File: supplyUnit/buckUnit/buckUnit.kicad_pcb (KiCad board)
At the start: 2 copper layers, 72.7 x 33.9 mm, 30 parts, among them J1 VBAT, J2 Motor, J3 Dribbler A, J4 Conn_01x05, J5 L1, J6 Conn_02x03_Counter_Clockwise, J7 Conn_02x03_Counter_Clockwise, J8 Dribbler B, Q1 BSC084P03NS3 G, Q2 BSC084P03NS3 G, Q3 IRLML6344TRPbF, SW1 SW_SPDT, U1 OKL-T6-W12-C, U2 OKL-T6-W12-C

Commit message: 死
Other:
- board text added: "JLCJLCJLCJLC"

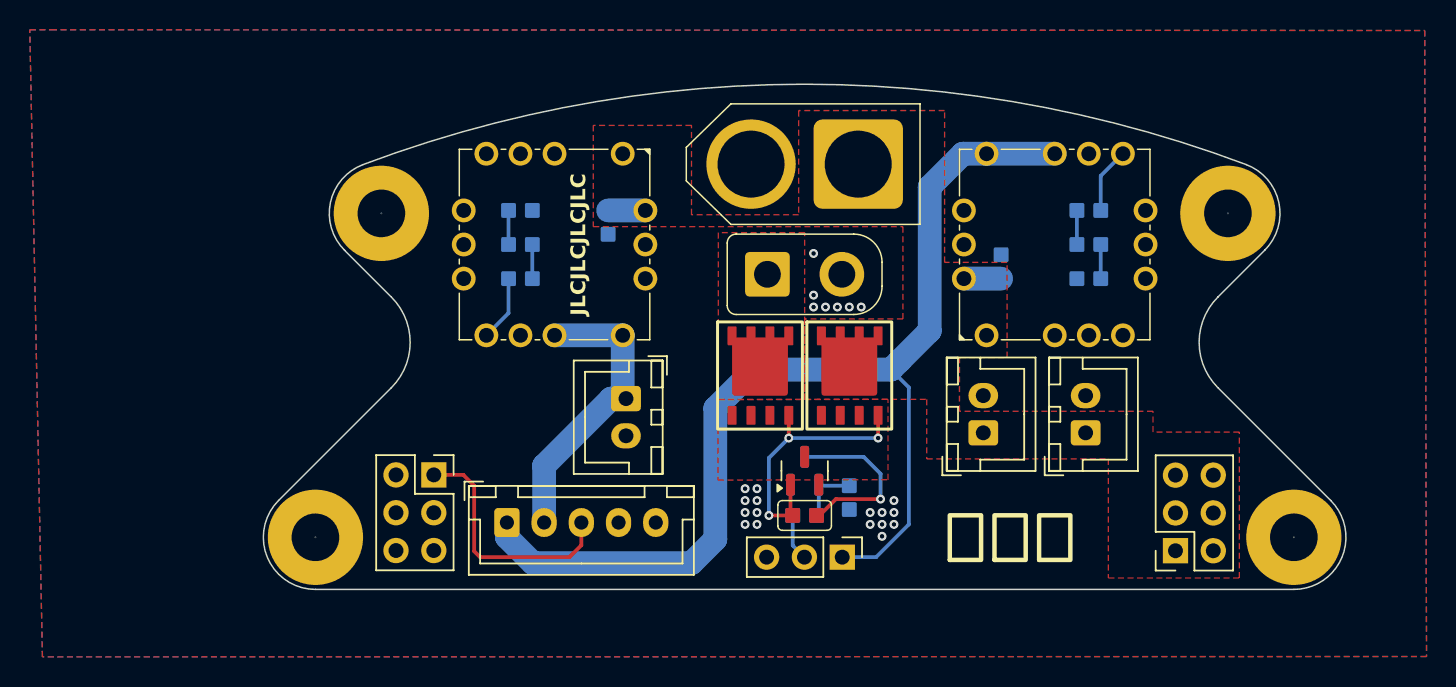
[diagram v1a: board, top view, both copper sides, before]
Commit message: 死 - 过杀 PMOS
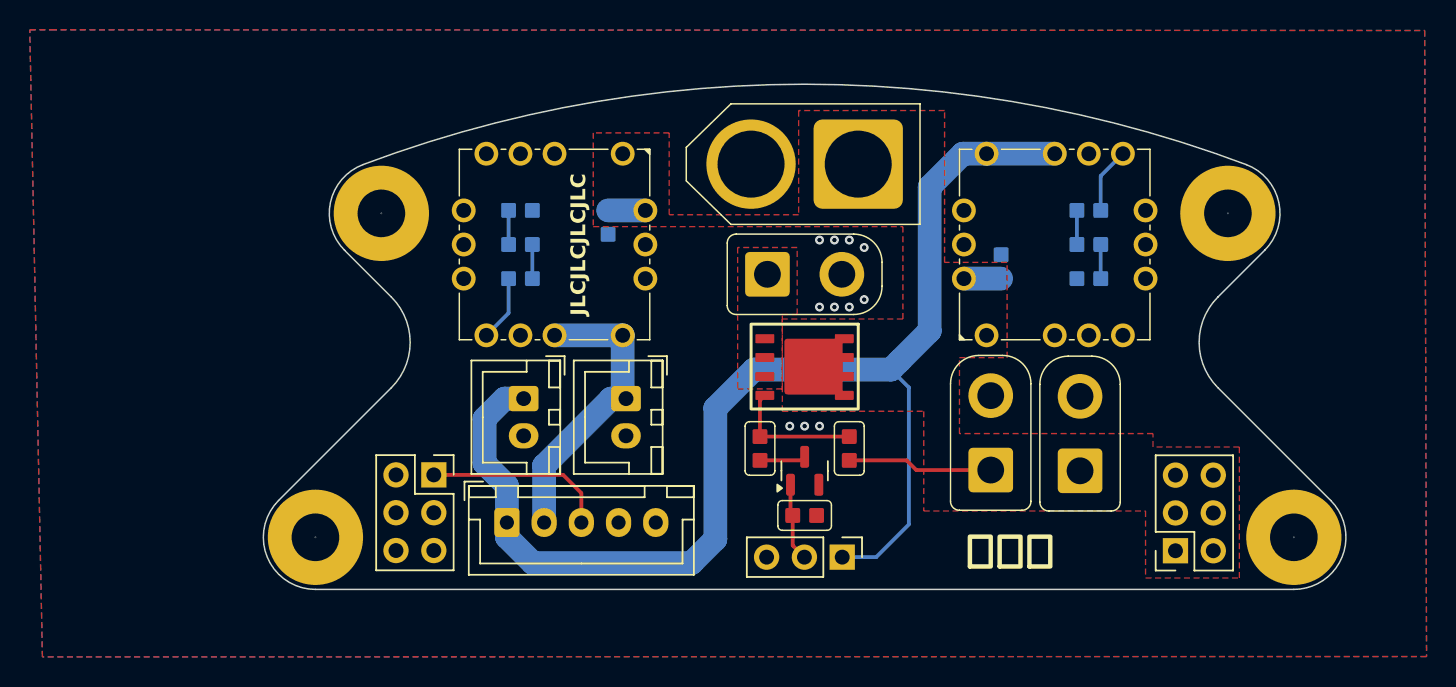
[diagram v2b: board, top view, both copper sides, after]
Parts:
- removed D1: BZX84C12, Package_TO_SOT_SMD:SOT-23
- removed Q3: IRLML6344TRPbF, Package_TO_SOT_SMD:SOT-23
- added J9: SPARE, Connector_JST:JST_XH_B2B-XH-A_1x02_P2.50mm_Vertical, F.Cu at (118.3, 105.5)
- J3, J8: footprint Connector_JST:JST_XH_B2B-XH-A_1x02_P2.50mm_Vertical -> Library:xt30-f
- Q2: value BSC084P03NS3 G -> IRLML6344TRPbF; footprint Library:8-DFN (5x6) -> Package_TO_SOT_SMD:SOT-23
- R8: value 10K -> 100; moved to F.Cu
- R9: moved to F.Cu
- moved Q2 7.07 mm to (137.2, 110.4), turned to 90 degrees
- moved R7 5.41 mm to (140.2, 108.9), turned to 90 degrees
- moved R8 5.41 mm to (134.2, 108.9), turned to -90 degrees
- moved R9 3.23 mm to (137.2, 113.4), turned to 0 degrees
- moved Q1 3.06 mm to (137.2, 103.4), turned to -90 degrees
- moved J3 0.50 mm to (149.7, 107.8)
- moved J8 0.38 mm to (155.7, 107.9)
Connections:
- Q1 pad 1: Net-(D1-K) -> +12V MOTOR
- Q1 pad 2: Net-(D1-K) -> +12V MOTOR
- Q1 pad 3: Net-(D1-K) -> +12V MOTOR
- Q1 pad 4: Net-(D1-A) -> Net-(Q1-G)
- Q2 pad 1: Net-(D1-K) -> Net-(Q2-G)
- Q2 pad 2: Net-(D1-K) -> GND
- Q2 pad 3: Net-(D1-K) -> Net-(Q2-D)
- R7 pad 1: Net-(D1-A) -> +12V
- R7 pad 2: Net-(Q3-D) -> Net-(Q1-G)
- R8 pad 1: Net-(SW1-B) -> Net-(Q1-G)
- R8 pad 2: Net-(Q3-G) -> Net-(Q2-D)
- R9 pad 1: Net-(Q3-G) -> Net-(Q2-G)
- SW1 pad 2: Net-(SW1-B) -> Net-(Q2-G)
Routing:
- net Net-(D1-A): track 18.3 -> 0.00 mm, vias 3 -> 0
- net Net-(Q3-D): track 12.1 -> 0.00 mm, vias 1 -> 0
- net +5V: track 77.0 -> 87.8 mm
- net +12V: track 5.00 -> 14.8 mm
- net Net-(Q1-G): track 0.00 -> 8.90 mm
- net Net-(Q2-G): track 0.00 -> 5.25 mm
- net /KICK SIG: track 16.6 -> 12.4 mm
- net Net-(Q3-G): track 3.90 -> 0.00 mm
- net Net-(SW1-B): track 3.13 -> 0.00 mm
- net Net-(Q2-D): track 0.00 -> 3.10 mm
- net GND: vias 23 -> 11
- removed copper zone on F.Cu, net Net-(D1-K)

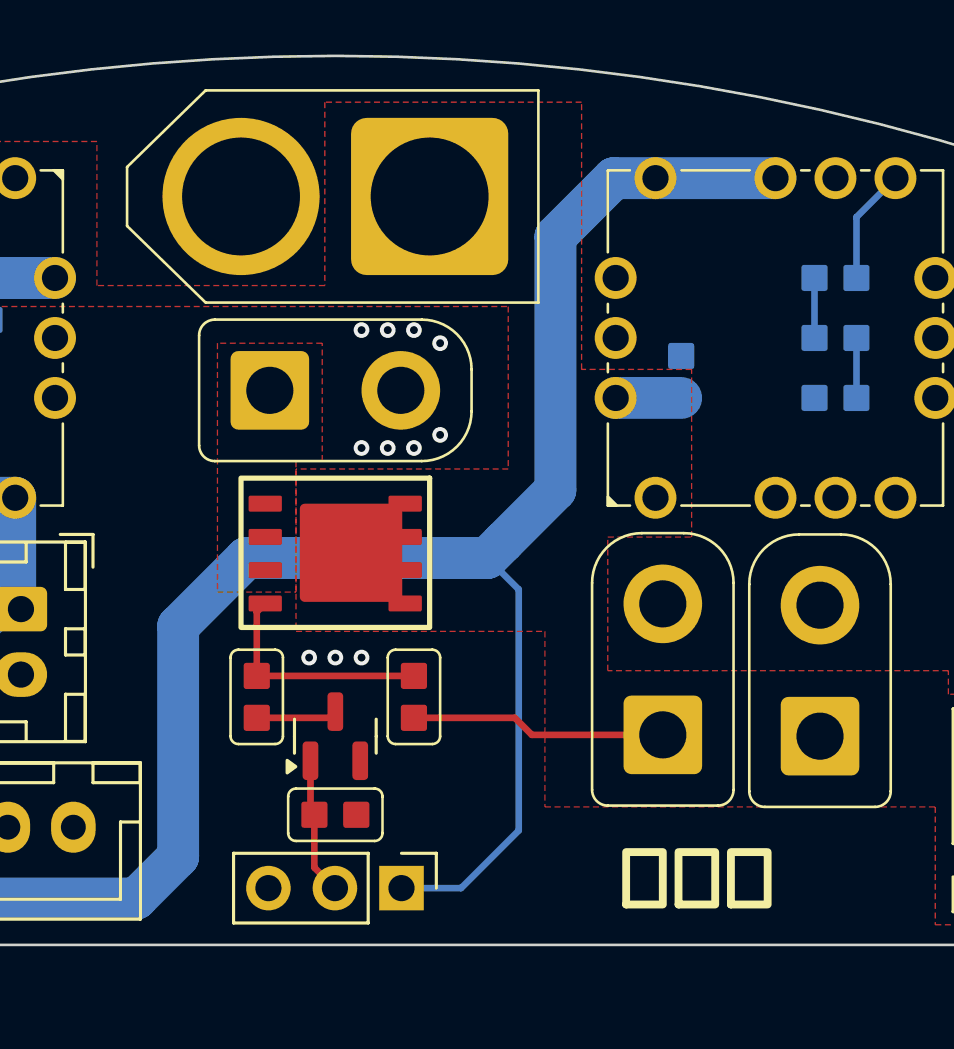
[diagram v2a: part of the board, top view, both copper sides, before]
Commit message: 死 - 过杀 PMOS
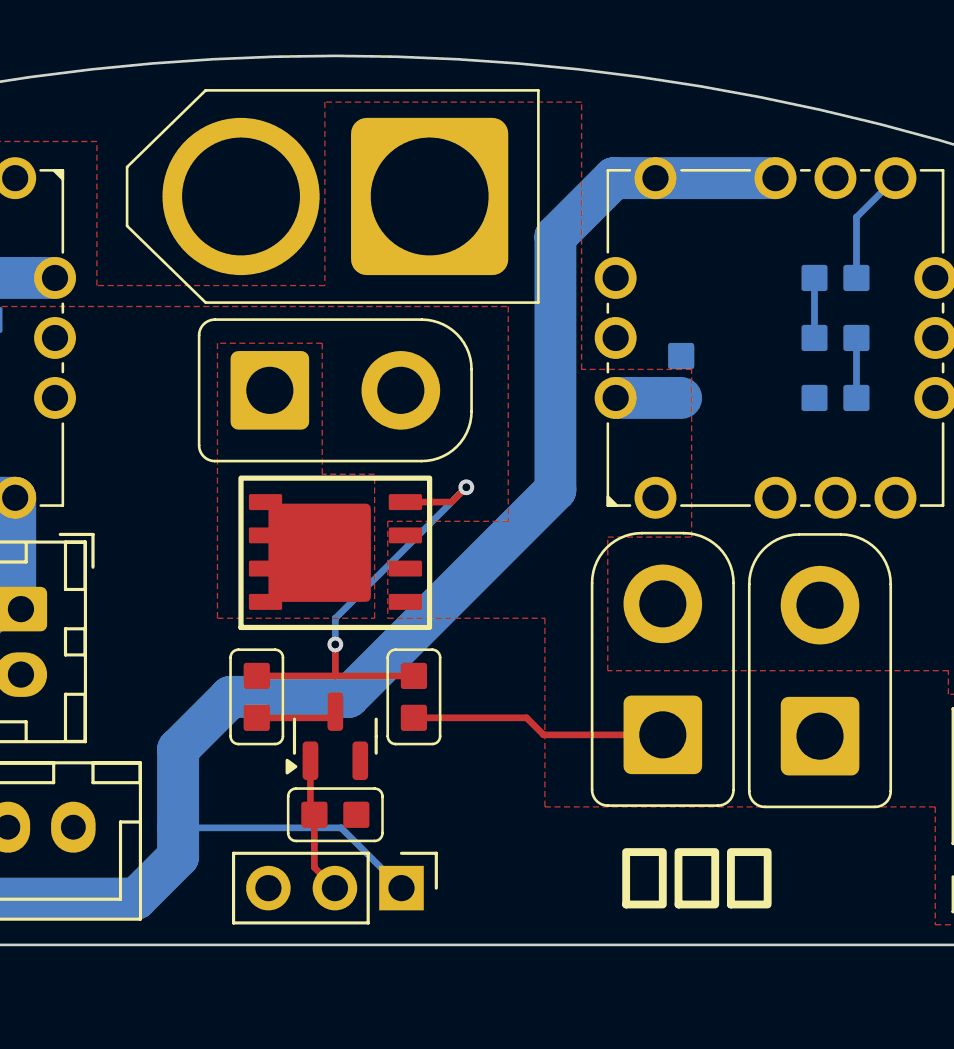
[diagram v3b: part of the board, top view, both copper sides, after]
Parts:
- R8: value 100 -> 1K
- U1, U2: value OKL-T6-W12-C -> OKL-T6-W12P-C
- turned Q1 to 90 degrees
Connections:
- Q1 pad 1: +12V MOTOR -> +12V
- Q1 pad 2: +12V MOTOR -> +12V
- Q1 pad 3: +12V MOTOR -> +12V
- Q1 pad 5: +12V -> +12V MOTOR
- Q1 pad 6: +12V -> +12V MOTOR
- Q1 pad 7: +12V -> +12V MOTOR
- Q1 pad 8: +12V -> +12V MOTOR
- Q1 pad 9: +12V -> +12V MOTOR
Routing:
- net +5V: track 87.8 -> 78.2 mm
- net Net-(Q1-G): track 8.90 -> 17.8 mm, vias 0 -> 2
- net GND: vias 11 -> 0

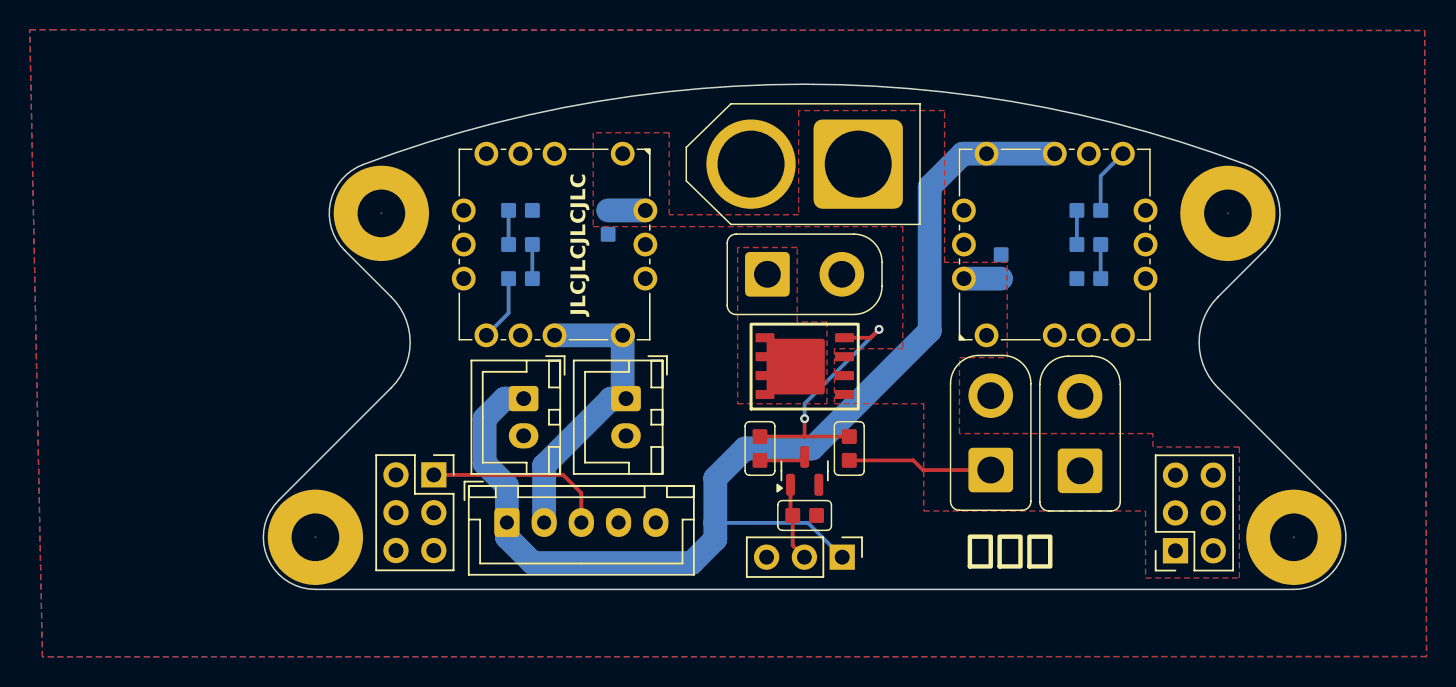
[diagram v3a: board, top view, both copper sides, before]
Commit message: Going to move to VNH
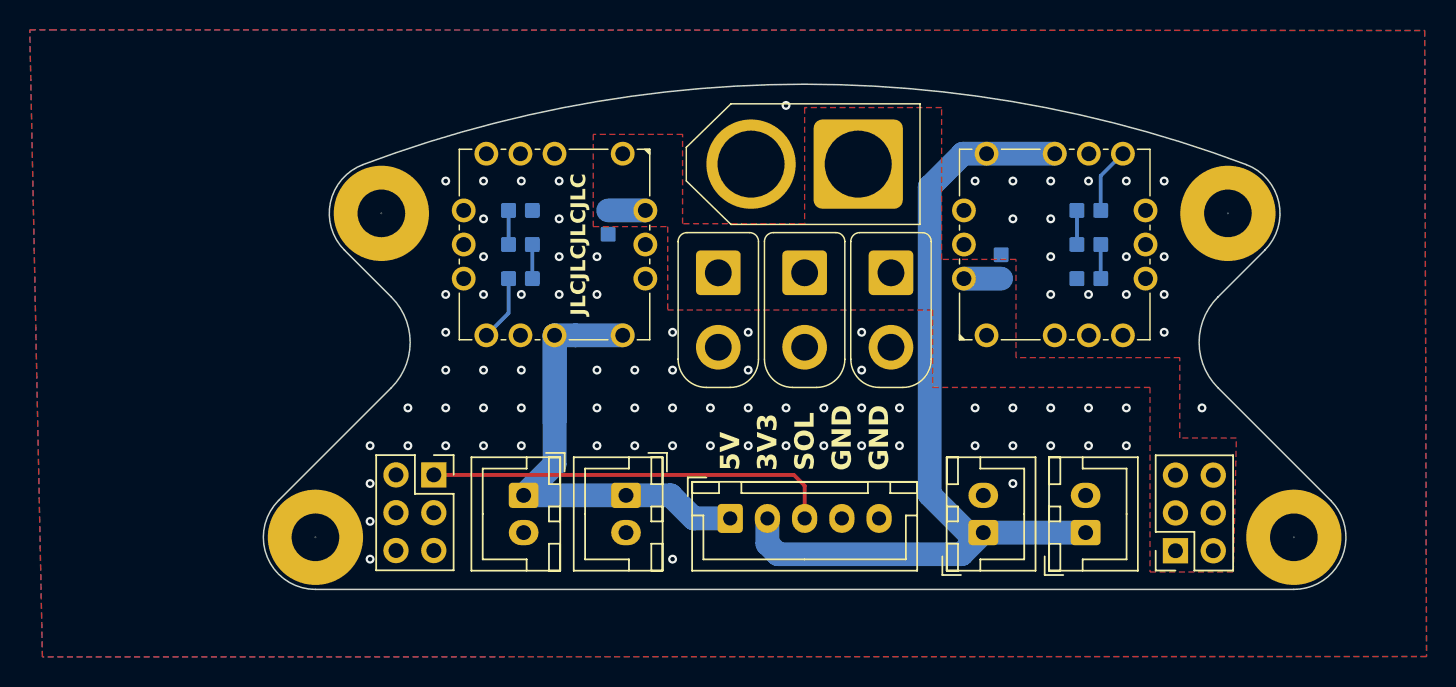
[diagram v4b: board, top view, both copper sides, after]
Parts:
- removed the J2 at (137.2, 97.2)
- removed the J3 at (149.7, 107.8)
- removed the J8 at (155.7, 107.9)
- removed Q1: BSC084P03NS3 G, Library:8-DFN (5x6)
- removed Q2: IRLML6344TRPbF, Package_TO_SOT_SMD:SOT-23
- removed R7, R9: 10K, Library:res0603
- removed R8: 1K, Library:res0603
- removed SW1: SW_SPDT, Connector_PinHeader_2.54mm:PinHeader_1x03_P2.54mm_Vertical
- added J10: SPARE, Connector_JST:JST_XH_B2B-XH-A_1x02_P2.50mm_Vertical, F.Cu at (156.1, 114.5)
- added J4: Motor, Library:xt30-f, F.Cu at (131.4, 99.6)
- added J5: Drib A, Library:xt30-f, F.Cu at (137.2, 99.6)
- added J6: Drib B, Library:xt30-f, F.Cu at (143.0, 99.6)
- added J9: L1, Connector_JST:JST_XH_B2B-XH-A_1x02_P2.50mm_Vertical, F.Cu at (149.2, 114.5)
- J1: renamed from J6; value Conn_02x03_Counter_Clockwise -> 12V
- J2: renamed from J7; value Conn_02x03_Counter_Clockwise -> GND
- J7: renamed from J9; value SPARE -> L1
- J8: renamed from J5; value L1 -> SPARE
- moved J11 15.0 mm to (132.2, 113.6)
- moved J7 6.50 mm to (118.3, 112.0)
- moved J8 6.50 mm to (125.2, 112.0)
- renumbered J4 to J11, J1 to J3
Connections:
- J11 pad 1: +5V -> +3V3
- J11 pad 2: +3V3 -> +5V
- J7 pad 1: +5V -> +3V3
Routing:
- net +5V: track 78.2 -> 58.6 mm
- net Net-(Q1-G): track 17.8 -> 0.00 mm, vias 2 -> 0
- net +3V3: track 20.1 -> 36.5 mm
- net /KICK SIG: track 12.4 -> 27.4 mm
- net +12V: track 14.8 -> 5.00 mm
- net Net-(Q2-G): track 5.25 -> 0.00 mm
- net Net-(Q2-D): track 3.10 -> 0.00 mm
- net GND: vias 0 -> 86
- removed copper zone on F.Cu, net +12V MOTOR
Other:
- board text added: "3V3"
- board text added: "5V"
- board text added: "GND"
- board text added: "SOL"
- board text removed: "高電圧"

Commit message: Fab
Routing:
- net +3V3: track 36.5 -> 30.7 mm
